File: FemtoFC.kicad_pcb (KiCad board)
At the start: 4 copper layers, 17.5 x 50.1 mm, 60 parts, among them J1 Power in, J2 Conn_01x02_Male, J3 Micro_SD_Card, J4 Pyro 2, J5 Pyro 1, P1 USB_C_Plug_USB2.0, Q1 FDS9926A, Q2 FDS4953, U1 USBLC6-2SC6, U2 3.3v REG, U3 ATSAMD21G18A-M, U4 W25Q128JVS, U5 LSM6DS3, U6 BMP280, Y1 Crystal

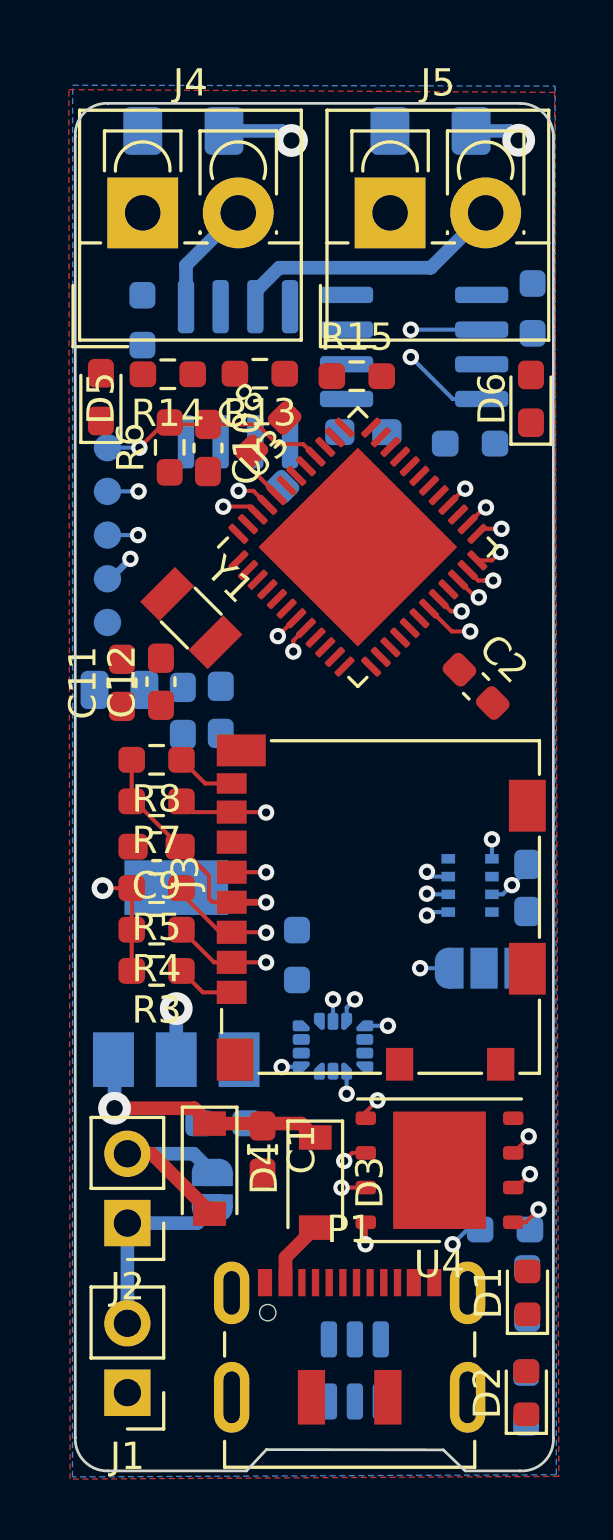
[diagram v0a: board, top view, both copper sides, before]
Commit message: 0.2
PCB edit
Added 3D models
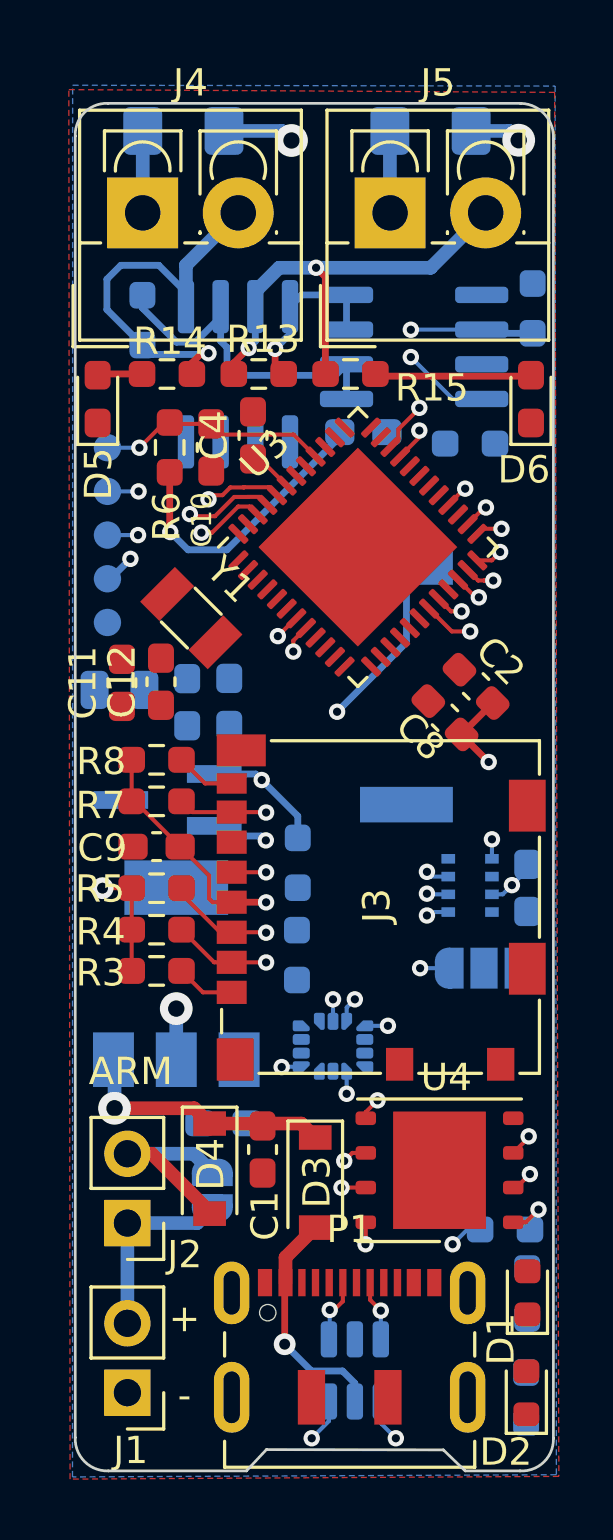
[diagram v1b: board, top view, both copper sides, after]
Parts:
- added BZ1: Buzzer, Buzzer_Beeper:Buzzer_Murata_PKMCS0909E, B.Cu at (182.0, 71.2)
- added Q3: NDT3055L, Package_TO_SOT_SMD:TSOT-23_HandSoldering, B.Cu at (173.3, 75.4)
- added R17: 10k, Resistor_SMD:R_0603_1608Metric_Pad0.98x0.95mm_HandSolder, B.Cu at (178.1, 77.7)
- C4: moved to F.Cu
- moved C8 12.2 mm to (183.4, 72.4), turned to 135 degrees
- moved C4 3.01 mm to (176.4, 62.1), turned to 90 degrees
- moved C6 0.42 mm to (175.5, 71.8)
- moved C5 0.36 mm to (174.0, 71.8)
- moved R15 0.24 mm to (180.0, 59.8)
- moved D5 0.14 mm to (170.7, 60.8)
- moved C10 0.12 mm to (174.9, 62.5)
- renumbered TP1 to GND, TP5 to RST, TP4 to SWCLK, TP3 to SWDIO, TP2 to VDD
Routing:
- net Net-(U1-Pad6): track 0.00 -> 50.7 mm, vias 0 -> 2
- net Net-(U1-Pad4): track 0.00 -> 50.7 mm, vias 0 -> 2
- net Net-(BZ1-Pad2): track 0.00 -> 16.1 mm, vias 0 -> 2
- net VDDIN: track 28.0 -> 42.5 mm, vias 14 -> 17
- net Net-(Q1-Pad5): track 0.00 -> 12.9 mm
- net Net-(J4-Pad2): track 4.23 -> 15.0 mm, vias 0 -> 1
- net Net-(J5-Pad2): track 10.2 -> 17.0 mm, vias 0 -> 2
- net Net-(Q1-Pad7): track 0.00 -> 6.34 mm, vias 0 -> 1
- net VBUS: track 2.47 -> 8.56 mm, vias 0 -> 1
- net Net-(D6-Pad2): track 0.00 -> 5.75 mm
- net Buzzer: track 0.00 -> 4.50 mm, vias 0 -> 1
- net Net-(F2-Pad2): track 0.00 -> 3.00 mm
- net Net-(F1-Pad2): track 0.00 -> 3.00 mm
- net Net-(P1-PadA6): track 0.00 -> 2.39 mm, vias 0 -> 1
- net Net-(P1-PadA7): track 0.00 -> 2.24 mm, vias 0 -> 1
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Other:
- board text added: "+"
- board text added: "-"
- board text added: "0x76"
- board text added: "0x77"
- board text added: "ARM"

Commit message: Rework for prototype 2
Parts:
- added R18: 1k, Resistor_SMD:R_0603_1608Metric_Pad0.98x0.95mm_HandSolder, F.Cu at (181.6, 72.3)
- moved R15 5.16 mm to (185.1, 60.8), turned to 90 degrees
- moved C8 2.54 mm to (185.7, 71.3), turned to 90 degrees
- moved R13 2.26 mm to (178.8, 60.2), turned to 45 degrees
- moved TP5 1.44 mm to (171.1, 61.1)
- moved TP4 1.08 mm to (171.1, 63.0)
- moved C7 0.84 mm to (180.4, 62.8)
- moved JP1 0.81 mm to (174.1, 89.7)
- moved TP3 0.72 mm to (171.1, 65.0)
- moved C11 0.63 mm to (171.1, 71.5)
- moved Y1 0.48 mm to (173.8, 68.4)
- moved C12 0.45 mm to (172.8, 71.5)
- moved J1 0.45 mm to (172.3, 97.1)
- moved C4 0.44 mm to (176.4, 61.6)
- moved C2 0.36 mm to (184.2, 71.3), turned to -90 degrees
- moved TP2 0.36 mm to (171.1, 67.0)
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- renumbered GND to TP1, VDD to TP2, SWDIO to TP3, SWCLK to TP4, RST to TP5
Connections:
- C2 pad 1: Net-(C2-Pad1) -> GNDANA
- U3 pad 11: unconnected-(U3-Pad11) -> VMeas
- U3 pad 18: Net-(C2-Pad1) -> GNDANA
- U3 pad 35: Net-(C2-Pad1) -> GNDANA
- U3 pad 42: Net-(C2-Pad1) -> GNDANA
- U3 pad 49: unconnected-(U3-Pad49) -> GNDANA
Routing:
- net SPI_CS_LSM: track 0.96 -> 23.6 mm
- net VDDIN: track 42.5 -> 65.0 mm, vias 17 -> 19
- net +BATT: track 61.3 -> 81.1 mm, vias 2 -> 4
- net VDD: track 9.59 -> 26.1 mm, vias 1 -> 3
- net MISO: track 28.6 -> 40.9 mm, vias 4 -> 5
- net VDDANA: track 0.00 -> 8.42 mm, vias 0 -> 1
- net Net-(C11-Pad2): track 0.00 -> 6.81 mm
- net Net-(J5-Pad2): track 17.0 -> 22.8 mm
- net Net-(C12-Pad2): track 0.00 -> 5.13 mm
- net VBUS: track 8.56 -> 13.6 mm
- net Net-(D6-Pad2): track 5.75 -> 1.60 mm
- net Net-(D2-Pad1): track 0.00 -> 2.82 mm, vias 0 -> 1
- net Net-(JP2-Pad2): track 0.00 -> 2.18 mm
- net Net-(D1-Pad1): track 0.00 -> 2.08 mm, vias 0 -> 1
- net MOSI: track 76.0 -> 78.1 mm
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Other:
- outline, holes or cut-outs redrawn
- board text added: "CLK"
- board text added: "GND"
- board text added: "RST"
- board text added: "SWDIO"
- board text added: "VDD"

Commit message: V3
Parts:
- removed D1, D2: G, LED_SMD:LED_0603_1608Metric
- removed FB1: FerriteBead_Small, Resistor_SMD:R_0805_2012Metric
- removed J2: Conn_01x02_Male, Connector_PinHeader_2.54mm:PinHeader_1x02_P2.54mm_Vertical
- removed JP1: SolderJumper_2_Open, Jumper:SolderJumper-2_P1.3mm_Open_RoundedPad1.0x1.5mm
- removed JP2: SolderJumper_3_Open, Jumper:SolderJumper-3_P1.3mm_Open_RoundedPad1.0x1.5mm
- removed TP1, TP2, TP3, TP4, TP5: TestPoint, TestPoint:TestPoint_Pad_D1.0mm
- added 3v3: G, LED_SMD:LED_0603_1608Metric, F.Cu at (81.7, 90.6)
- added 3v3: TestPoint, TestPoint:TestPoint_Pad_D1.0mm, B.Cu at (81.0, 61.3)
- added C14: 220uF 16V, Capacitor_Tantalum_SMD:CP_EIA-7343-31_Kemet-D, F.Cu at (92.0, 81.5)
- added C15: 1uF, Capacitor_SMD:C_0402_1005Metric_Pad0.74x0.62mm_HandSolder, B.Cu at (84.1, 83.5)
- added GND: TestPoint, TestPoint:TestPoint_Pad_D1.0mm, B.Cu at (81.0, 63.4)
- added RST: TestPoint, TestPoint:TestPoint_Pad_D1.0mm, B.Cu at (81.0, 55.2)
- added SWCLK: TestPoint, TestPoint:TestPoint_Pad_D1.0mm, B.Cu at (81.0, 57.2)
- added SWDIO: TestPoint, TestPoint:TestPoint_Pad_D1.0mm, B.Cu at (81.0, 59.3)
- added VDD: G, LED_SMD:LED_0603_1608Metric, F.Cu at (81.7, 87.5)
- C1: value 100nF -> 10uf; footprint Capacitor_SMD:C_0603_1608Metric_Pad1.08x0.95mm_HandSolder -> Capacitor_SMD:C_0402_1005Metric_Pad0.74x0.62mm_HandSolder; moved to B.Cu
- C10, C11, C12, C3, C8: footprint Capacitor_SMD:C_0603_1608Metric_Pad1.08x0.95mm_HandSolder -> Capacitor_SMD:C_0402_1005Metric_Pad0.74x0.62mm_HandSolder
- C13, C5, C6, C7: footprint Capacitor_SMD:C_0603_1608Metric_Pad1.08x0.95mm_HandSolder -> Capacitor_SMD:C_0402_1005Metric_Pad0.74x0.62mm_HandSolder; moved to F.Cu
- C2: value 10uF -> 1uF; footprint Capacitor_SMD:C_0603_1608Metric_Pad1.08x0.95mm_HandSolder -> Capacitor_SMD:C_0402_1005Metric_Pad0.74x0.62mm_HandSolder
- C4: value 100nF -> 1uF; footprint Capacitor_SMD:C_0603_1608Metric_Pad1.08x0.95mm_HandSolder -> Capacitor_SMD:C_0402_1005Metric_Pad0.74x0.62mm_HandSolder
- C9: value 100nF -> 10uF; footprint Capacitor_SMD:C_0603_1608Metric_Pad1.08x0.95mm_HandSolder -> Capacitor_SMD:C_0402_1005Metric_Pad0.74x0.62mm_HandSolder; moved to B.Cu
- J3: moved to B.Cu
- J4: footprint TerminalBlock_4Ucon:TerminalBlock_4Ucon_1x02_P3.50mm_Vertical -> TerminalBlock_Phoenix:TerminalBlock_Phoenix_MPT-0,5-2-2.54_1x02_P2.54mm_Horizontal
- J5: value Pyro 1 -> Pyro 2; footprint TerminalBlock_4Ucon:TerminalBlock_4Ucon_1x02_P3.50mm_Vertical -> TerminalBlock_Phoenix:TerminalBlock_Phoenix_MPT-0,5-2-2.54_1x02_P2.54mm_Horizontal
- Q3: footprint Package_TO_SOT_SMD:TSOT-23_HandSoldering -> Package_TO_SOT_SMD:TSOT-23; moved to F.Cu
- R1, R10, R11, R12, R14, R15, R2, R5, R6, R7: footprint Resistor_SMD:R_0603_1608Metric_Pad0.98x0.95mm_HandSolder -> Resistor_SMD:R_0402_1005Metric_Pad0.72x0.64mm_HandSolder
- R13, R18, R3, R4, R8: footprint Resistor_SMD:R_0603_1608Metric_Pad0.98x0.95mm_HandSolder -> Resistor_SMD:R_0402_1005Metric_Pad0.72x0.64mm_HandSolder; moved to B.Cu
- R16, R17, R9: footprint Resistor_SMD:R_0603_1608Metric_Pad0.98x0.95mm_HandSolder -> Resistor_SMD:R_0402_1005Metric_Pad0.72x0.64mm_HandSolder; moved to F.Cu
- U5, U6: moved to F.Cu
- moved D6 106.3 mm to (81.2, 46.6), turned to -90 degrees
- moved R1 105.0 mm to (81.7, 87.5), turned to 0 degrees
- moved C8 105.0 mm to (81.8, 56.4), turned to 180 degrees
- moved R2 104.9 mm to (81.7, 90.6), turned to 0 degrees
- moved R15 103.6 mm to (82.5, 46.1), turned to -90 degrees
- moved C13 102.9 mm to (88.8, 46.4), turned to 0 degrees
- moved C2 100.3 mm to (84.3, 63.2), turned to -135 degrees
- moved U6 100.2 mm to (88.8, 48.5)
- moved F2 98.7 mm to (84.5, 44.0), turned to 0 degrees
- moved J5 96.5 mm to (85.8, 41.3), turned to 180 degrees
- moved R16 96.0 mm to (83.3, 65.5), turned to -135 degrees
- moved U5 95.8 mm to (84.8, 69.0), turned to 90 degrees
- moved R9 95.3 mm to (92.4, 71.3)
- moved U4 95.3 mm to (90.3, 68.0)
- moved R10 94.9 mm to (89.8, 53.4), turned to 180 degrees
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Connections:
- C13 pad 1: VDDIN -> VDDANA
- C2 pad 1: GNDANA -> AREF
- C2 pad 2: VDDIN -> GNDANA
- C3 pad 1: VDDIN -> VDDANA
- C7 pad 1: VDDIN -> VDDANA
- C8 pad 1: VDDIN -> VDDANA
- C9 pad 1: VDDIN -> VDDANA
- D5 pad 1: GNDANA -> Net-(D5-Pad1)
- D6 pad 1: GNDANA -> Net-(D6-Pad1)
- F1 pad 1: +BATT -> Net-(F1-Pad1)
- F1 pad 2: Net-(F1-Pad2) -> Net-(D5-Pad1)
- F2 pad 1: +BATT -> Net-(F2-Pad1)
- F2 pad 2: Net-(F2-Pad2) -> Net-(D6-Pad1)
- J1 pad 2: Net-(J1-Pad2) -> +BATT
- J3 pad 4: VDDIN -> VDDANA
- J4 pad 1: Net-(F1-Pad2) -> Net-(D5-Pad1)
- J4 pad 2: Net-(J4-Pad2) -> GNDANA
- J5 pad 1: Net-(F2-Pad2) -> Net-(D6-Pad1)
- J5 pad 2: Net-(J5-Pad2) -> GNDANA
- P1 pad S1: GNDANA -> unconnected-(P1-PadS1)
- Q1 pad 2: P1_EN -> P2_EN
- Q1 pad 4: P2_EN -> P1_EN
- Q1 pad 5: Net-(Q1-Pad5) -> Net-(Q2-Pad4)
- Q1 pad 6: Net-(Q1-Pad5) -> Net-(Q2-Pad4)
- Q1 pad 7: Net-(Q1-Pad7) -> Net-(Q2-Pad2)
- Q1 pad 8: Net-(Q1-Pad7) -> Net-(Q2-Pad2)
- Q2 pad 1: Net-(J4-Pad2) -> +BATT
- Q2 pad 2: Net-(Q1-Pad5) -> Net-(Q2-Pad2)
- Q2 pad 3: Net-(J5-Pad2) -> +BATT
- Q2 pad 4: Net-(Q1-Pad7) -> Net-(Q2-Pad4)
- Q2 pad 5: GNDANA -> Net-(F2-Pad1)
- Q2 pad 6: GNDANA -> Net-(F2-Pad1)
- Q2 pad 7: GNDANA -> Net-(F1-Pad1)
- Q2 pad 8: GNDANA -> Net-(F1-Pad1)
- R12 pad 1: Net-(Q1-Pad5) -> Net-(Q2-Pad2)
- R12 pad 2: Net-(J4-Pad2) -> +BATT
- R13 pad 1: Net-(Q1-Pad7) -> Net-(Q2-Pad4)
- R13 pad 2: Net-(J5-Pad2) -> +BATT
- R14 pad 1: Net-(J4-Pad2) -> +BATT
- R15 pad 1: Net-(J5-Pad2) -> +BATT
- R16 pad 1: VDDIN -> VDDANA
- R3 pad 2: VDDIN -> VDDANA
- R4 pad 2: VDDIN -> VDDANA
- R5 pad 2: VDDIN -> VDDANA
- R6 pad 1: VDDIN -> VDDANA
- R7 pad 2: VDDIN -> VDDANA
- R8 pad 2: VDDIN -> VDDANA
- R9 pad 1: VDDIN -> VDDANA
- U2 pad 2: VDDIN -> VDDANA
- U3 pad 10: unconnected-(U3-Pad10) -> A4
- U3 pad 13: unconnected-(U3-Pad13) -> Buzzer
- U3 pad 14: unconnected-(U3-Pad14) -> D3
- U3 pad 17: VDDIN -> VDDANA
- U3 pad 19: P2_EN -> MOSI
- U3 pad 20: P1_EN -> SCK
- U3 pad 21: unconnected-(U3-Pad21) -> MISO
- U3 pad 22: SPI_CS_FLASH -> unconnected-(U3-Pad22)
- U3 pad 25: MOSI -> unconnected-(U3-Pad25)
- U3 pad 26: SCK -> unconnected-(U3-Pad26)
- U3 pad 27: unconnected-(U3-Pad27) -> P1_EN
- U3 pad 28: MISO -> P2_EN
- U3 pad 3: unconnected-(U3-Pad3) -> A0
- U3 pad 31: unconnected-(U3-Pad31) -> SDA
- U3 pad 32: unconnected-(U3-Pad32) -> SCL
- U3 pad 36: VDDIN -> VDDANA
- U3 pad 37: unconnected-(U3-Pad37) -> FLASH_MOSI
- U3 pad 38: unconnected-(U3-Pad38) -> FLASH_SCK
- U3 pad 39: unconnected-(U3-Pad39) -> SPI_CS_FLASH
- U3 pad 4: unconnected-(U3-Pad4) -> AREF
- U3 pad 44: VDDIN -> VDDANA
- U3 pad 48: unconnected-(U3-Pad48) -> FLASH_MISO
- U3 pad 7: SDA -> unconnected-(U3-Pad7)
- U3 pad 8: SCL -> unconnected-(U3-Pad8)
- U3 pad 9: unconnected-(U3-Pad9) -> A3
- U4 pad 2: MISO -> FLASH_MISO
- U4 pad 3: VDDIN -> VDDANA
- U4 pad 5: MOSI -> FLASH_MOSI
- U4 pad 6: SCK -> FLASH_SCK
- U4 pad 7: VDDIN -> VDDANA
- U4 pad 8: VDDIN -> VDDANA
- U5 pad 5: VDDIN -> VDDANA
- U5 pad 8: VDDIN -> VDDANA
- U6 pad 2: VDDIN -> VDDANA
- U6 pad 5: Net-(JP2-Pad2) -> GNDANA
- U6 pad 6: VDDIN -> VDDANA
- U6 pad 8: VDDIN -> VDDANA
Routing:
- net VDDIN: track 65.0 -> 0.00 mm, vias 19 -> 0
- net VDDANA: track 8.42 -> 69.9 mm, vias 1 -> 12
- net MOSI: track 78.1 -> 23.4 mm, vias 4 -> 2
- net SCK: track 65.6 -> 24.4 mm, vias 4 -> 2
- net FLASH_MISO: track 0.00 -> 31.8 mm, vias 0 -> 2
- net Net-(J5-Pad2): track 22.8 -> 0.00 mm, vias 2 -> 0
- net SCL: track 29.0 -> 8.22 mm, vias 2 -> 0
- net FLASH_SCK: track 0.00 -> 17.4 mm, vias 0 -> 2
- net MISO: track 40.9 -> 23.9 mm, vias 5 -> 2
- net SDA: track 26.3 -> 9.59 mm, vias 2 -> 0
- net FLASH_MOSI: track 0.00 -> 15.7 mm, vias 0 -> 2
- net Net-(J4-Pad2): track 15.0 -> 0.00 mm, vias 1 -> 0
- net Buzzer: track 4.50 -> 18.8 mm, vias 1 -> 2
- net SPI_CS_FLASH: track 29.1 -> 42.5 mm
- net Net-(Q2-Pad4): track 0.00 -> 13.1 mm
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- added copper zone on B.Cu, net +BATT
- added copper zone on F.Cu, net +BATT
- added copper zone on In2.Cu, net GNDANA
- added copper zone on In1.Cu, net VDDANA
- removed copper zone on In2.Cu, net VDDIN
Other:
- board size 17.5 x 50.1 mm -> 15 x 56 mm
- board text removed: "0x76"
- board text removed: "0x77"
- board text removed: "ARM"
- board text removed: "CLK"
- board text removed: "GND"
- board text removed: "RST"
- board text removed: "SWDIO"
- board text removed: "VDD"

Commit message: Rev 27052023
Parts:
- removed C1: 10uf, Capacitor_SMD:C_0402_1005Metric_Pad0.74x0.62mm_HandSolder
- removed C11, C12: 22pF, Capacitor_SMD:C_0402_1005Metric_Pad0.74x0.62mm_HandSolder
- removed Y1: Crystal, Crystal:Crystal_SMD_3215-2Pin_3.2x1.5mm
- added D7: APA102-2020, LED_SMD:LED-APA102-2020, F.Cu at (86.8, 76.5)
- added R19: 10k, Resistor_SMD:R_0402_1005Metric_Pad0.72x0.64mm_HandSolder, F.Cu at (90.1, 49.2)
- added R20: 10k, Resistor_SMD:R_0402_1005Metric_Pad0.72x0.64mm_HandSolder, F.Cu at (90.1, 51.5)
- moved C7 1.60 mm to (88.5, 51.8), turned to 90 degrees
- moved U6 0.97 mm to (87.9, 48.3)
- moved C2 0.90 mm to (83.6, 62.5)
- moved C13 0.89 mm to (88.0, 46.1)
- moved R9 0.63 mm to (92.4, 71.9)
- moved R5 0.62 mm to (86.0, 73.0)
- moved R16 0.61 mm to (83.6, 66.1), turned to 180 degrees
- moved R7 0.52 mm to (86.1, 71.8)
- moved U4 0.17 mm to (90.5, 67.9)
- moved C10 0.16 mm to (83.6, 54.0)
- moved C8 0.14 mm to (81.8, 56.5)
- moved R17 0.13 mm to (91.5, 48.6)
- moved C6 0.09 mm to (84.9, 64.8)
- moved C5 0.06 mm to (85.7, 64.0)
- renumbered VDD to D1, 3v3 to D2, GND to TP1, 3v3 to TP2, SWDIO to TP3, SWCLK to TP4, RST to TP5
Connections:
- C14 pad 1: VDD -> GNDANA
- D1 pad 2: VDD -> GNDANA
- D3 pad 1: VDD -> GNDANA
- D4 pad 1: VDD -> GNDANA
- U2 pad 3: VDD -> GNDANA
- U3 pad 1: Net-(C11-Pad2) -> CI
- U3 pad 2: Net-(C12-Pad2) -> DI
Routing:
- net GNDANA: track 1.41 -> 25.7 mm, vias 5 -> 22
- net CI: track 0.00 -> 23.7 mm
- net VDD: track 22.7 -> 0.00 mm, vias 2 -> 0
- net DI: track 0.00 -> 21.1 mm
- net VDDANA: track 69.9 -> 76.2 mm, vias 12 -> 13
- net Net-(C11-Pad2): track 5.41 -> 0.00 mm
- net Net-(C12-Pad2): track 4.71 -> 0.00 mm
- net +BATT: track 85.6 -> 83.3 mm, vias 10 -> 11
- net P1_EN: track 16.3 -> 14.7 mm
- net Net-(U1-Pad4): track 62.4 -> 61.1 mm
- net SCL: track 8.22 -> 7.25 mm
- net Net-(Q1-Pad5): track 13.1 -> 12.2 mm
- net SPI_CS_LSM: track 20.8 -> 21.5 mm
- net SDA: track 9.59 -> 10.1 mm
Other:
- board text added: "3V3"
- board text added: "APO"
- board text added: "GND"
- board text added: "MAIN"
- board text added: "RST"
- board text added: "SWCLK"
- board text added: "SWDIO"
- board text added: "VDD"
